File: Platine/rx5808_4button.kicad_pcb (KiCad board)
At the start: 2 copper layers, 80 x 65 mm, 62 parts, among them IC1 ATMEGA328-A, P1 CONN_01X02, P10 CONN_01X01, P11 CONN_01X01, P2 CONN_01X05, P3 CONN_02X03, P4 CONN_01X02, P5 BNC, P6 BNC, P7 CONN_01X02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

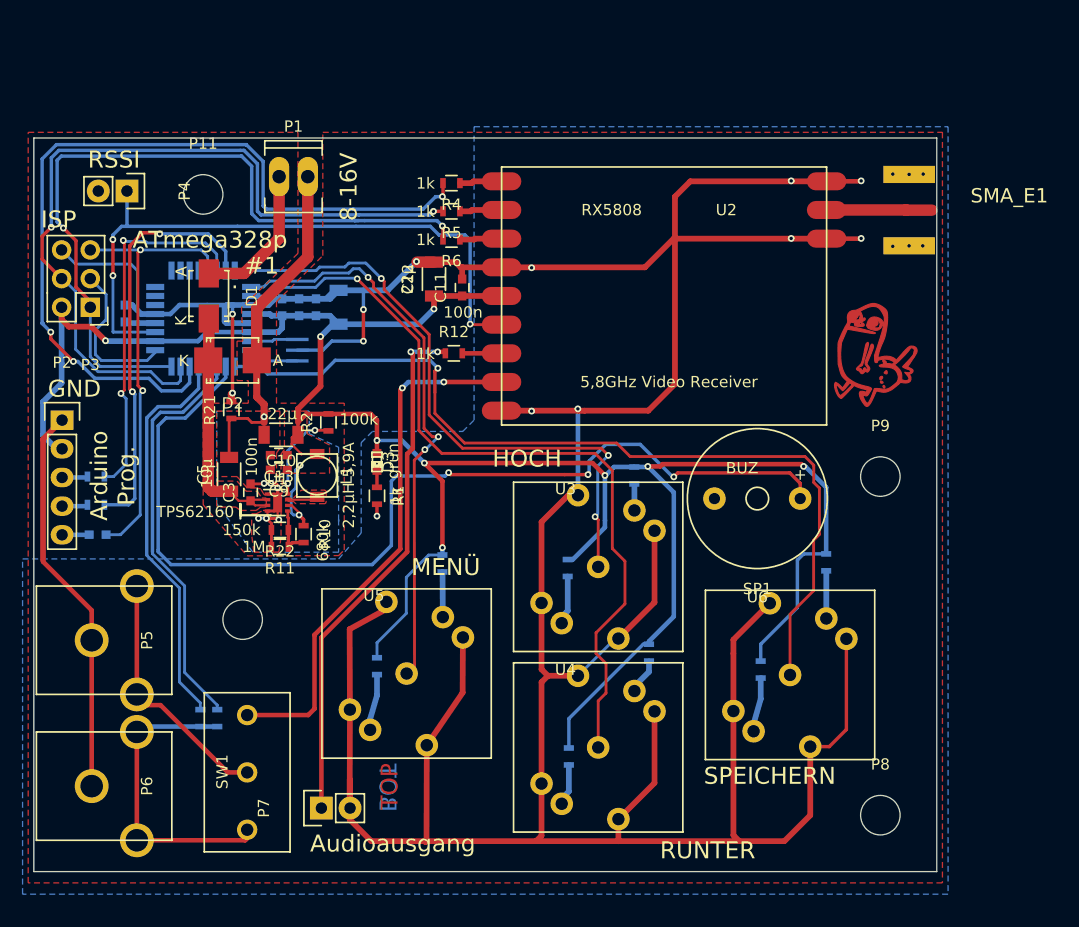
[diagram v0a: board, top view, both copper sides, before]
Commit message: neue LIB für den micromatchstecker
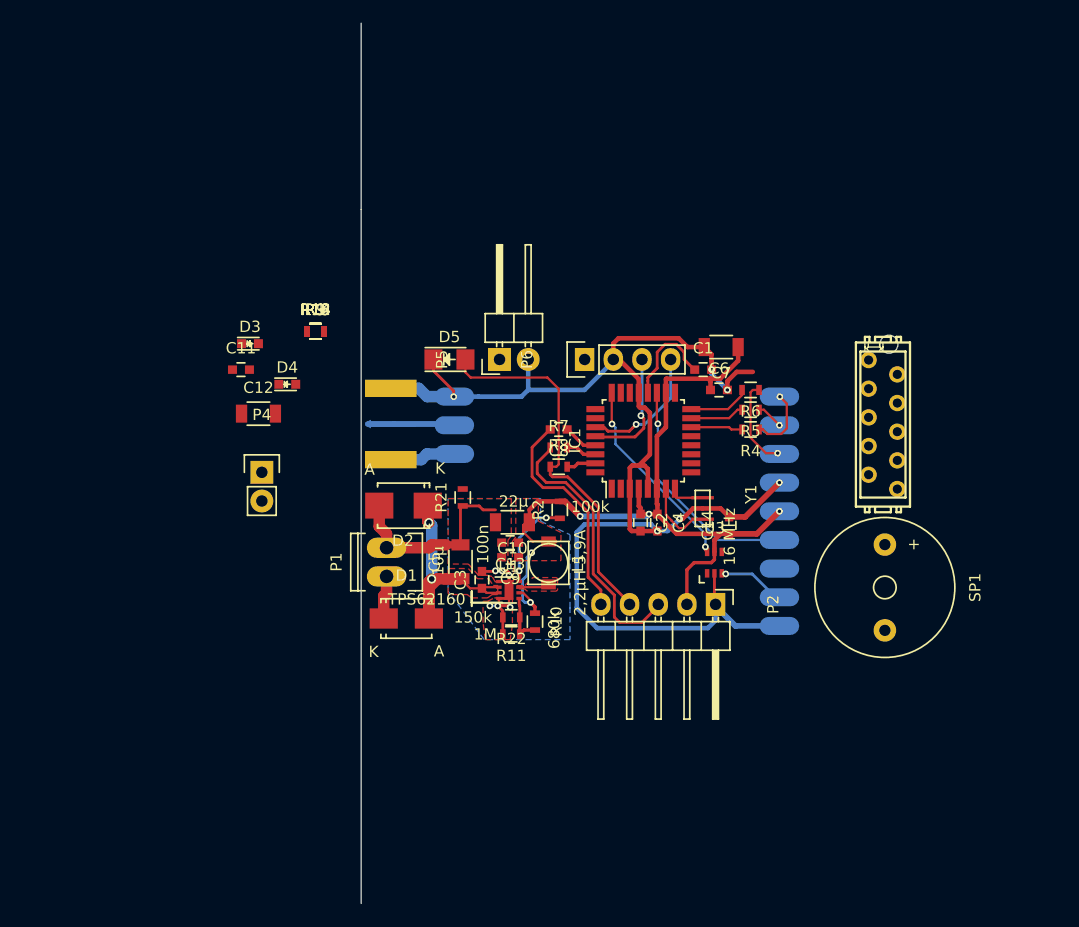
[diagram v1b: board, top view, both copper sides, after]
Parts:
- removed G***: LOGO, Dickbutt:Kupferdickbutt
- removed P10, P11, P8, P9: CONN_01X01, Mounting_Holes:MountingHole_3-5mm
- removed P3: CONN_02X03, Pin_Headers:Pin_Header_Straight_2x03
- removed R16, R17, R18, R19, R20: 220, Resistors_SMD:R_0603
- removed SW1: SWITCH_INV, Apem:2543xN
- removed U4, U5, U6: RF15-Punktlicht, Rafi:RF15-Punktlicht
- added C14: 100n, Capacitors_SMD:C_0603, F.Cu at (145.6, 113.5)
- added D4: grün, LEDs:LED_0603, F.Cu at (106.5, 101.0)
- added D5: IR_EMITTER, LEDs:LED_1206, F.Cu at (120.8, 98.8)
- C1, C2, C4, C6, C7, C8, IC1, R7, Y1: moved to F.Cu
- D1: value SB130 -> B 140 F; footprint Diodes_SMD:Diode-SMA_Standard -> Diodes_SMD:SMA_Standard
- D2: value TVS 18V -> P6SMB 18A SMD; footprint Diodes_SMD:Diode-SMB_Standard -> Diodes_SMD:SMB_Standard
- D3: footprint LEDs:LED-0603 -> LEDs:LED_0603
- P2: footprint Pin_Headers:Pin_Header_Straight_1x05 -> Pin_Headers:Pin_Header_Angled_1x05
- P5: footprint Cinch_angled_mono -> Pin_Headers:Pin_Header_Angled_1x02
- P6: value BNC -> CONN_01X04; footprint RCA:Cinch_angled_mono -> Pin_Headers:Pin_Header_Straight_1x04
- P7: value CONN_01X02 -> CONN_02X05; footprint Pin_Headers:Pin_Header_Straight_1x02 -> spezifisch:con-amp-micromatch-MICROMATCH-10
- R1: value 1k -> 1M
- R12: value 1k -> 220
- R13, R14, R15: value 220 -> 1k; moved to F.Cu
- R3: value 1k -> 1M; moved to F.Cu
- R8: value 1k -> 220; moved to F.Cu
- R9: value 470 -> 220; moved to F.Cu
- SMA_E1, U2: moved to B.Cu
- U3: value RF15-Punktlicht -> sn74lvc1g3157; footprint Rafi:RF15-Punktlicht -> TO_SOT_Packages_SMD:SC-70-6
- moved SMA_E1 66.4 mm to (106.8, 103.2), turned to 180 degrees
- moved P7 60.3 mm to (159.2, 104.6)
- moved P2 60.2 mm to (144.4, 120.5), turned to 270 degrees
- moved P6 57.8 mm to (132.8, 98.8), turned to 90 degrees
- moved C1 51.5 mm to (143.3, 99.7), turned to 0 degrees
- moved P5 43.9 mm to (125.3, 98.8), turned to 90 degrees
- moved C8 41.9 mm to (130.5, 105.0)
- moved R8 41.1 mm to (130.5, 108.3)
- moved R7 41.1 mm to (130.5, 106.6)
- moved R15 41.0 mm to (109.0, 96.3), turned to 0 degrees
- moved IC1 40.5 mm to (138.0, 106.0), turned to 90 degrees
- moved Y1 38.6 mm to (143.2, 112.0), turned to 270 degrees
- moved C2 37.0 mm to (137.8, 113.2), turned to 270 degrees
- moved C4 37.0 mm to (139.2, 113.2), turned to 270 degrees
- moved C6 36.4 mm to (144.7, 101.5), turned to 0 degrees
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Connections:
- net /Funk_clk renamed /Funk1_clk
- net /Funk_data renamed /Funk1_data
- net /Funk_ss renamed /Funk1_ss
- D2 pad 1: GNDPWR -> +12V
- D2 pad 2: +12V -> GNDPWR
- D3 pad 1: +5V -> GND
- IC1 pad 14: Net-(IC1-Pad14) -> /ss
- IC1 pad 17: /sck -> /led3
- IC1 pad 19: /rssi -> /rssi1
- IC1 pad 22: Net-(IC1-Pad22) -> /rssi2
- IC1 pad 23: Net-(IC1-Pad23) -> /led1
- IC1 pad 24: Net-(IC1-Pad24) -> /led2
- IC1 pad 27: Net-(IC1-Pad27) -> /sda
- IC1 pad 28: Net-(IC1-Pad28) -> /scl
- IC1 pad 9: /save -> Net-(IC1-Pad9)
- P4 pad 1: /rssi -> /rssi1
- P6 pad 1: /VideoOut -> +5V
- P7 pad 1: Net-(P7-Pad1) -> +5V
- R1 pad 1: Net-(D3-Pad2) -> /rssi1
- R12 pad 1: Net-(P7-Pad1) -> Net-(D3-Pad2)
- R12 pad 2: Net-(R12-Pad2) -> /led1
- R13 pad 1: Net-(R13-Pad1) -> /Funk2_data
- R13 pad 2: +5V -> /ss
- R14 pad 1: Net-(R14-Pad1) -> /Funk2_ss
- R14 pad 2: +5V -> /mosi
- R15 pad 1: Net-(R15-Pad1) -> /Funk2_clk
- R15 pad 2: +5V -> /miso
- R3 pad 1: /VideoOut -> /rssi2
- R3 pad 2: Net-(IC1-Pad13) -> GND
- R4 pad 2: Net-(IC1-Pad14) -> /ss
- R9 pad 1: /VideoOut -> Net-(D4-Pad2)
- R9 pad 2: Net-(IC1-Pad11) -> /led3
- U2 pad 10: Net-(R12-Pad2) -> /Audio1
- U2 pad 11: Net-(SW1-Pad1) -> /Video1
- U2 pad 9: /rssi -> /rssi1
- U3 pad 1: /up -> /Video2
- U3 pad 3: Net-(R13-Pad1) -> /Video1
- U3 pad 4: GND -> Net-(P5-Pad1)
- U3 pad 5: Net-(R14-Pad1) -> +5V
- U3 pad 6: GND -> /led2
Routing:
- net GND: track 414.5 -> 127.1 mm, vias 19 -> 6
- net +5V: track 229.4 -> 73.6 mm, vias 11 -> 5
- net /buzzer: track 88.9 -> 0.00 mm, vias 3 -> 0
- net /save: track 78.5 -> 0.00 mm, vias 1 -> 0
- net Net-(IC1-Pad14): track 74.7 -> 0.00 mm, vias 3 -> 0
- net /down: track 71.1 -> 0.00 mm, vias 1 -> 0
- net /mosi: track 70.4 -> 4.81 mm, vias 2 -> 0
- net /miso: track 67.1 -> 5.47 mm, vias 2 -> 0
- net /rssi: track 58.3 -> 0.00 mm, vias 3 -> 0
- net /up: track 55.5 -> 0.00 mm, vias 3 -> 0
- net /mode: track 50.5 -> 0.00 mm, vias 3 -> 0
- net Net-(P7-Pad1): track 47.0 -> 0.00 mm, vias 2 -> 0
- net Net-(SW1-Pad1): track 46.9 -> 0.00 mm, vias 2 -> 0
- net /reset: track 39.5 -> 3.08 mm, vias 2 -> 0
- net Net-(IC1-Pad11): track 36.3 -> 0.00 mm
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- removed copper zone on B.Cu, net GND
- removed copper zone on F.Cu, net GND
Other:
- board outline removed
- rule via_min_size: 0.5 -> 0.6
- board text removed: "#1"
- board text removed: "."
- board text removed: "8-16V"
- board text removed: "ATmega328p"
- board text removed: "Arduino Prog."
- board text removed: "Audioausgang"
- board text removed: "BOT"
- board text removed: "Design verfügbar auf Github:"
- board text removed: "GND"
- board text removed: "HOCH"
- board text removed: "ISP"
- board text removed: "MENÜ"
- board text removed: "RSSI"
- board text removed: "RUNTER"
- board text removed: "SPEICHERN"
- board text removed: "TOP"
- board text removed: "https://github.com/Virtex7/RX5808"

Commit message: Platine fertig und exportiert.
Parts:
- removed C11: 100n, Capacitors_SMD:C_0603
- removed P4: CONN_01X02, Pin_Headers:Pin_Header_Straight_1x02
- added U4: MCPL3-BC-V, PhilippsFootprints:MCPL3-AC-V, F.Cu at (158.9, 102.6)
- L1: value 2,2µH 5,9A -> 2,2µH 1,5A; footprint TDK_Inductor:VLF4012A -> NR3015:NR3015
- SMA_E1: footprint SMA_EDGE:SMA_EDGE -> PhilippsFootprints:SMA_EDGE_small; moved to F.Cu
- moved D3 47.1 mm to (150.2, 97.8), turned to 270 degrees
- moved D4 46.2 mm to (152.5, 97.8), turned to 270 degrees
- moved R1 43.7 mm to (147.0, 117.8), turned to 270 degrees
- moved R9 43.3 mm to (152.1, 100.4), turned to 180 degrees
- moved R15 41.0 mm to (147.5, 110.3), turned to 180 degrees
- moved R12 40.6 mm to (149.4, 100.0), turned to 180 degrees
- moved R14 40.5 mm to (147.5, 108.7), turned to 180 degrees
- moved R13 40.0 mm to (147.5, 107.1), turned to 180 degrees
- moved C12 36.6 mm to (138.3, 116.1), turned to 180 degrees
- moved R3 22.6 mm to (130.5, 103.0), turned to 180 degrees
- moved P7 13.4 mm to (155.8, 117.5)
- moved SP1 3.05 mm to (161.7, 117.0)
- moved SMA_E1 2.65 mm to (106.7, 105.9)
- moved D5 2.30 mm to (120.8, 96.5)
- moved L1 0.80 mm to (129.4, 117.6)
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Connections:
- SP1 pad 1: /buzzer -> +5V
- SP1 pad 2: GND -> /buzzer
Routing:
- net GND: track 127.1 -> 185.0 mm, vias 6 -> 9
- net /rssi2: track 0.00 -> 43.4 mm, vias 0 -> 2
- net Net-(P5-Pad1): track 0.00 -> 39.3 mm, vias 0 -> 4
- net +5V: track 73.6 -> 106.4 mm, vias 5 -> 6
- net /buzzer: track 0.00 -> 28.9 mm
- net /up: track 0.00 -> 26.8 mm, vias 0 -> 2
- net /mode: track 0.00 -> 25.8 mm, vias 0 -> 2
- net /down: track 0.00 -> 23.4 mm, vias 0 -> 2
- net /led2: track 17.6 -> 39.0 mm, vias 2 -> 3
- net /led1: track 0.00 -> 17.8 mm, vias 0 -> 2
- net /Video2: track 0.00 -> 14.9 mm, vias 0 -> 1
- net /Funk2_clk: track 0.00 -> 12.1 mm
- net /led3: track 0.00 -> 12.0 mm, vias 0 -> 2
- net /Funk2_ss: track 0.00 -> 10.8 mm
- net /Funk2_data: track 0.00 -> 10.1 mm
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- added copper zone on B.Cu, net GND
- added copper zone on F.Cu, net GND
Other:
- board outline added: 50.5 x 29.5 mm
- net class Default: clearance 0.2032 -> 0.2; trace_width 0.3048 -> 0.25
- rule trace_clearance: 0.2032 -> 0.2
- rule trace_min: 0.1524 -> 0.15
- board text added: "328PB"
- board text added: "Antenne"
- board text added: "FPV-RX5823 1/2"
- board text added: "mega"

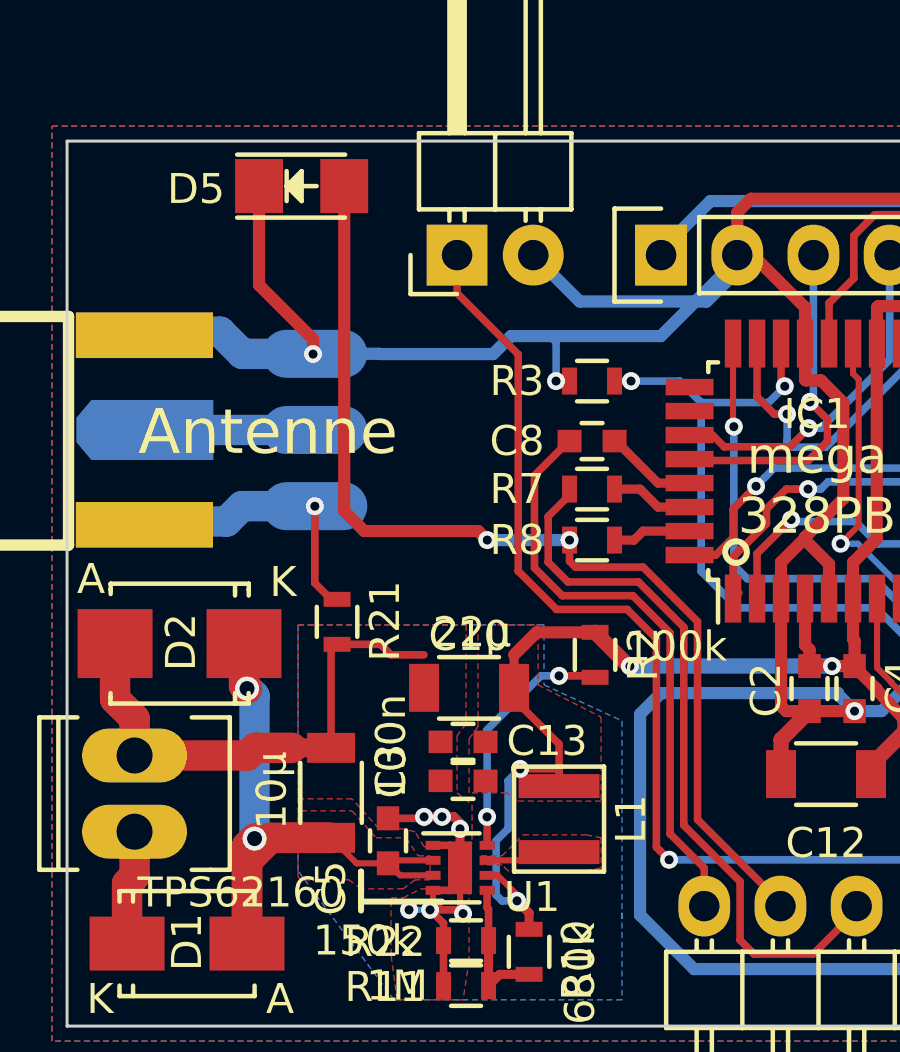
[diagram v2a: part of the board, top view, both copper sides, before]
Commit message: Layout fertig. Überprüfung steht aus.
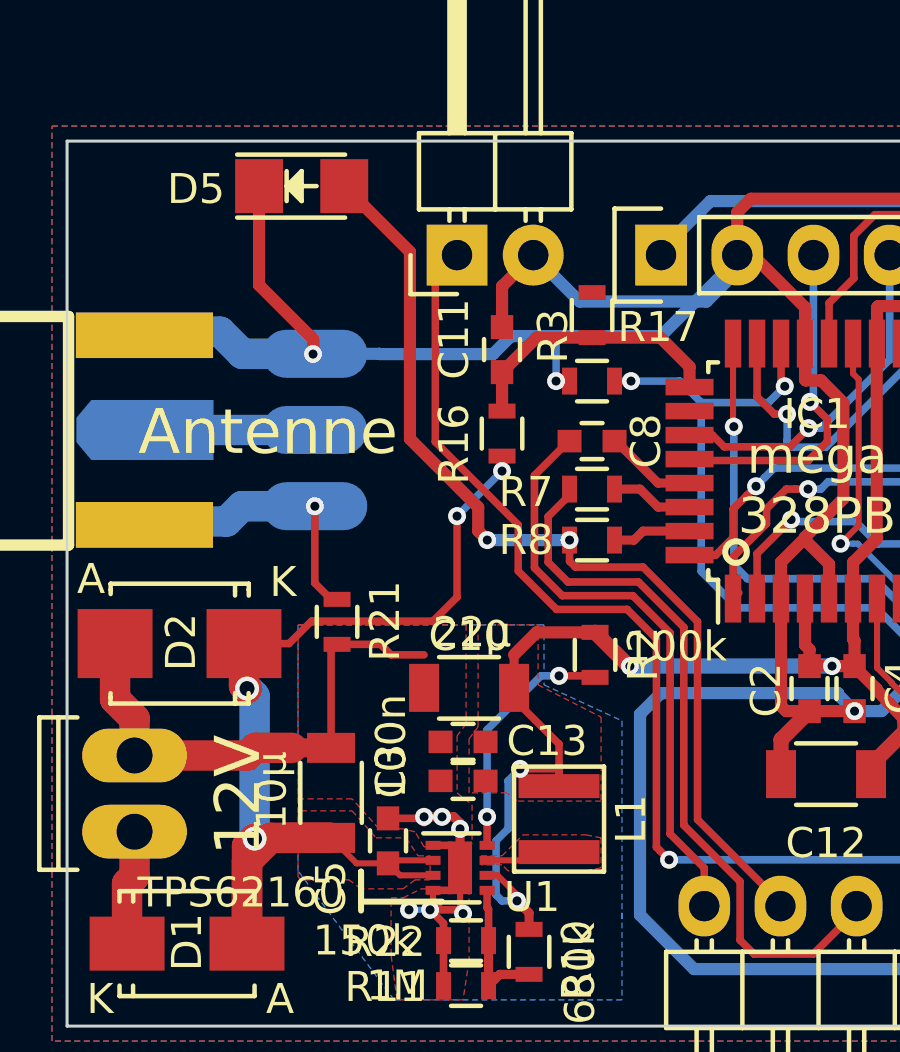
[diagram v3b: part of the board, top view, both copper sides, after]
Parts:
- added C11: 100n, Capacitors_SMD:C_0603, F.Cu at (127.5, 102.0)
- added R16: 15k, Resistors_SMD:R_0603, F.Cu at (127.5, 104.8)
- added R17: 1k, Resistors_SMD:R_0603, F.Cu at (130.5, 100.8)
- P7: footprint spezifisch:con-amp-micromatch-MICROMATCH-10 -> PhilippsFootprints:MICROMATCH-10
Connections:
- IC1 pad 25: Net-(IC1-Pad25) -> /adc_12V
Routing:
- net +12V: track 24.6 -> 37.6 mm, vias 2 -> 4
- net /adc_12V: track 0.00 -> 9.11 mm
- net GND: track 185.0 -> 187.9 mm
- net /txd: track 36.0 -> 33.7 mm
- net Net-(P5-Pad1): track 39.3 -> 39.9 mm
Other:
- board text added: "12V"
